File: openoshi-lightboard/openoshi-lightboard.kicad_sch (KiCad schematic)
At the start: 26 parts, among them J1 USB_C_Receptacle_PowerOnly_6P, Q1 CSD16301Q2, Q2 CSD16301Q2, Q3 CSD16301Q2, Q4 CSD16301Q2, SW1 SW_Push, SW2 SW_Push, U1 CH32V003FxUx, U2 TLV61070ADBV, U3 MCP73831-3-MC

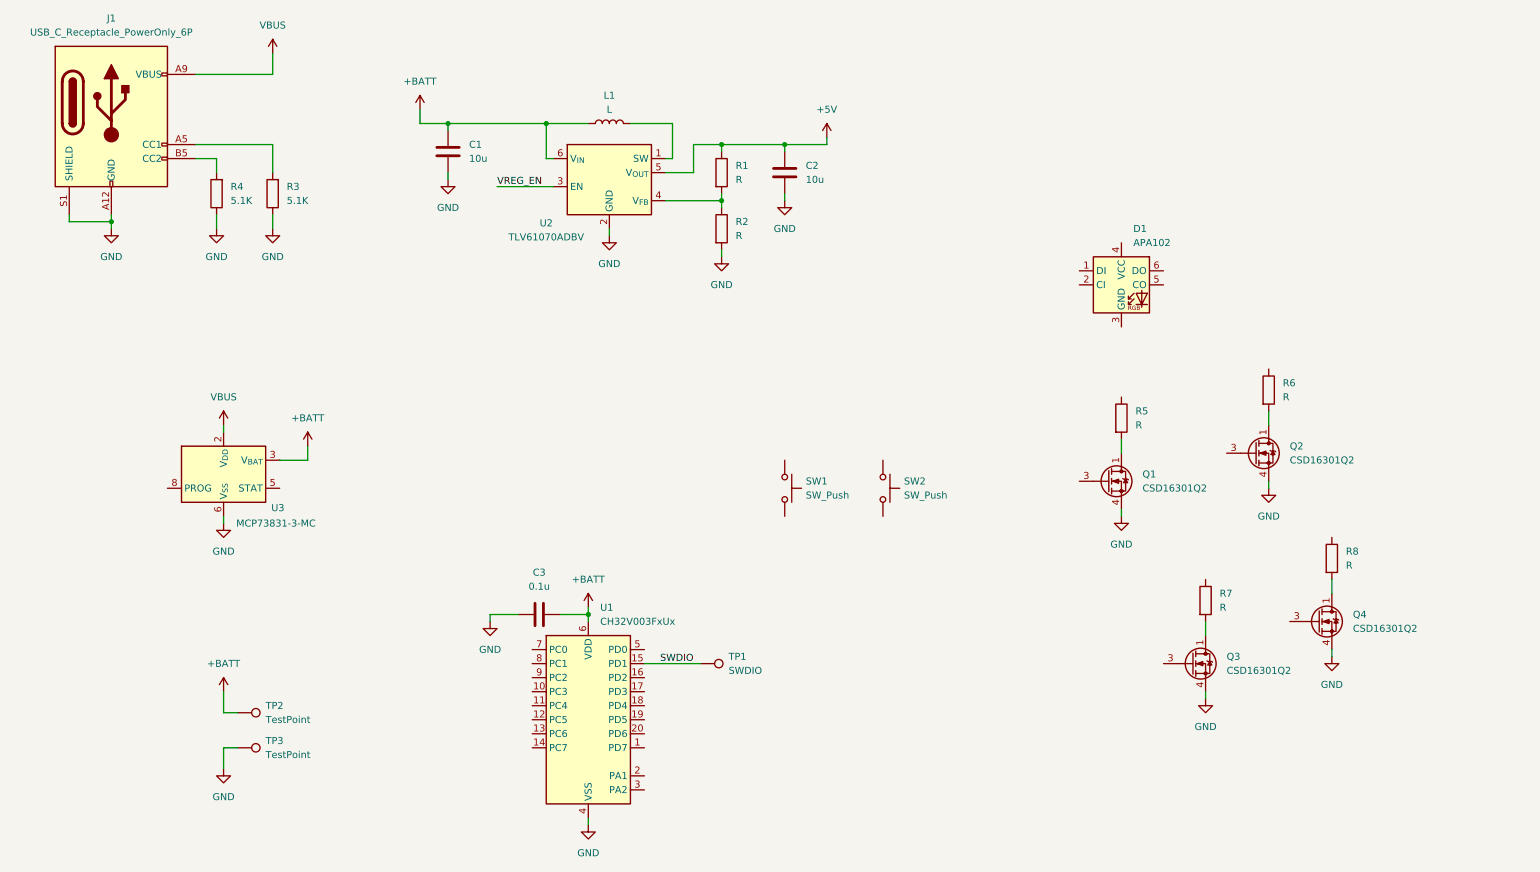
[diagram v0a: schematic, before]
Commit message: updated readme and part names
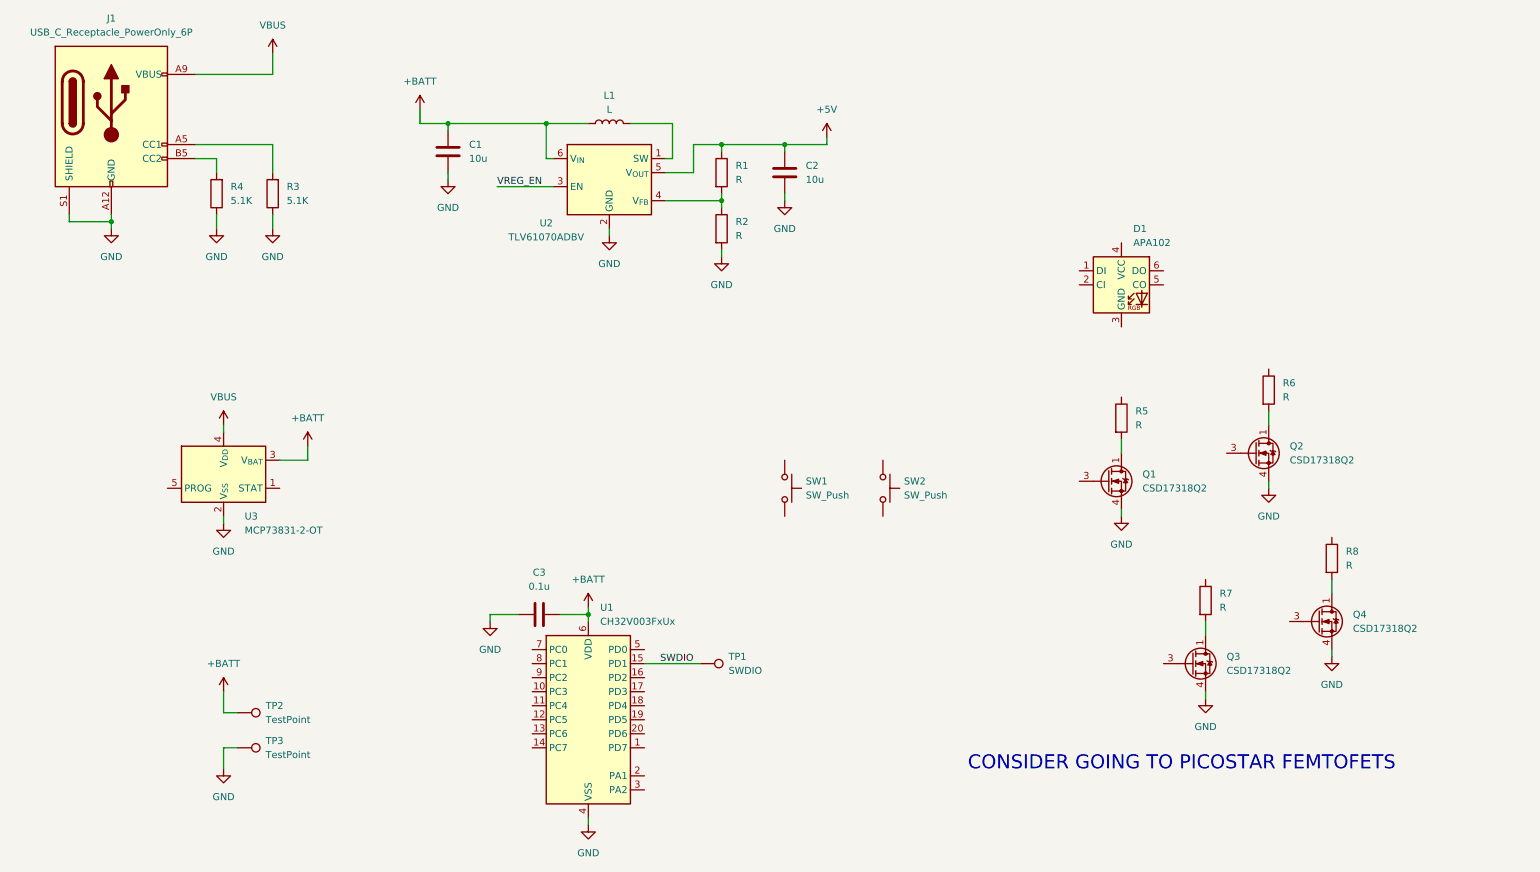
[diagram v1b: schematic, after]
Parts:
- removed U3: MCP73831-3-MC, Package_DFN_QFN:DFN-8-1EP_3x2mm_P0.5mm_EP1.7x1.4mm, symbol Battery_Management:MCP73831-3-MC
- added U3: MCP73831-2-OT, Package_TO_SOT_SMD:SOT-23-5, symbol Battery_Management:MCP73831-2-OT
- Q1, Q2, Q3, Q4: value CSD16301Q2 -> CSD17318Q2
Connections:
- net +BATT: now also U3.3 (V_{BAT})
- net GND: now also U3.2 (V_{SS})
- net VBUS: now also U3.4 (V_{DD})
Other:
- note added: "CONSIDER GOING TO PICOSTAR FEMTOFETS"

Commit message: added LED
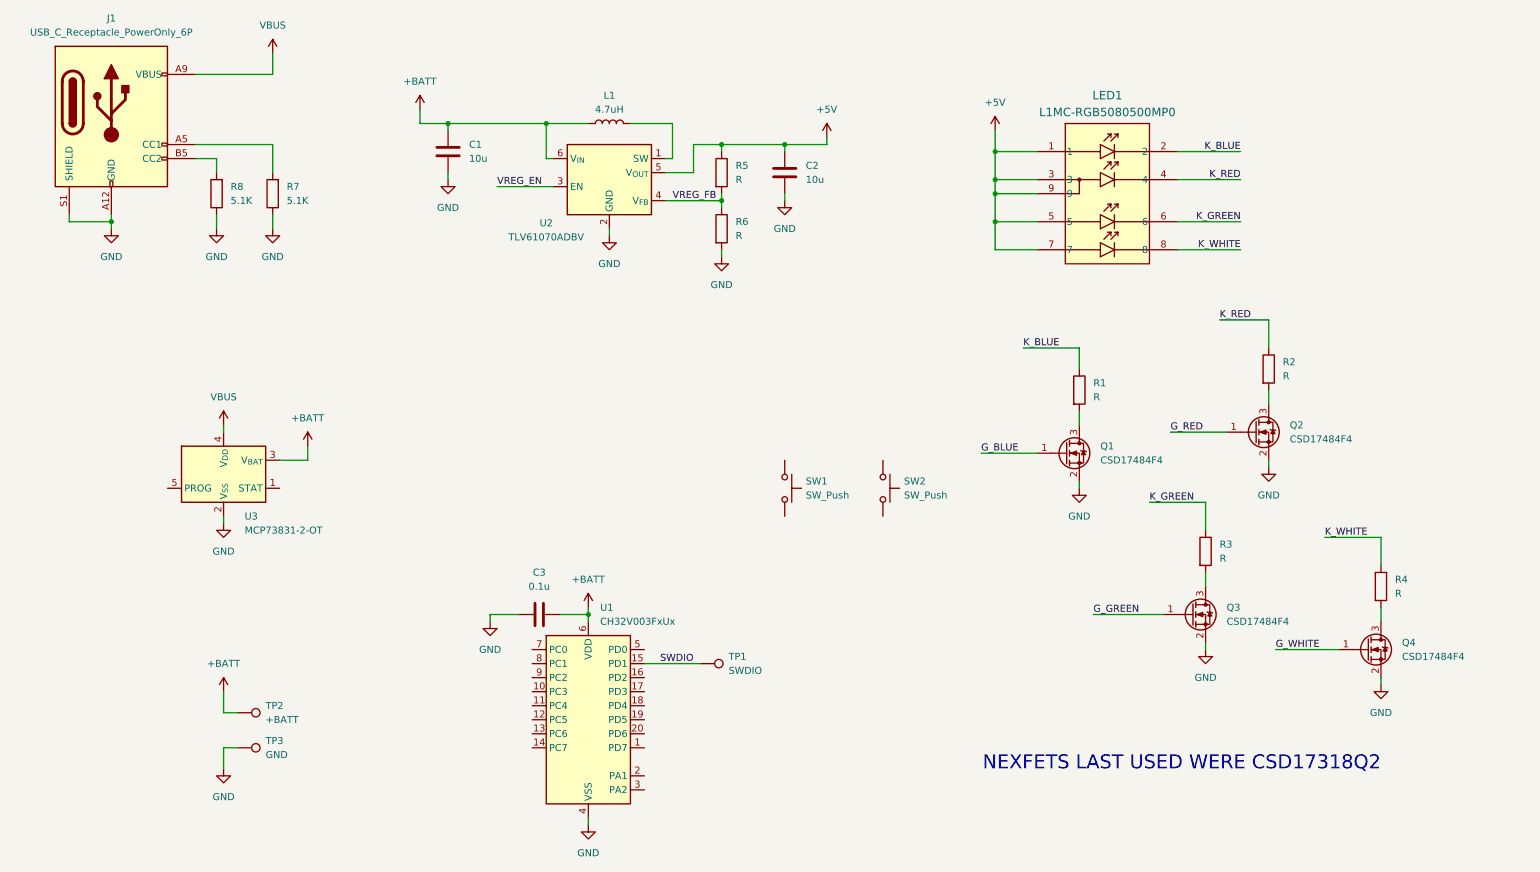
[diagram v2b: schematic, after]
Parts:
- removed D1: APA102, LED_SMD:LED_RGB_5050-6, symbol LED:APA102
- removed Q1, Q2, Q3, Q4: CSD17318Q2, Package_SON:Texas_DQK, symbol Transistor_FET:CSD16301Q2
- added LED1: L1MC-RGB5080500MP0, openoshi-lightboard:5050RGBW_LUL, symbol openoshi-lightboard:L1MC-RGB5080500MP0
- added Q1, Q2, Q3, Q4: CSD17484F4, Package_DFN_QFN:Texas_PicoStar_DFN-3_0.69x0.60mm, symbol Transistor_FET:CSD13380F3
- L1: value L -> 4.7uH
- TP2: value TestPoint -> +BATT; footprint TestPoint:TestPoint_Keystone_5019_Miniature -> Connector_Wire:SolderWirePad_1x01_SMD_5x10mm
- TP3: value TestPoint -> GND; footprint TestPoint:TestPoint_Keystone_5019_Miniature -> Connector_Wire:SolderWirePad_1x01_SMD_5x10mm
- renumbered R5 to R1, R6 to R2, R7 to R3, R8 to R4, R1 to R5, R2 to R6, R3 to R7, R4 to R8
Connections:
- net +5V: now also LED1.1, LED1.3, LED1.5, LED1.7, LED1.9
- net GND: now also Q1.2 (S), Q2.2 (S), Q3.2 (S), Q4.2 (S)
- net K_WHITE: now reaches R4.1
- net K_WHITE: now also LED1.8
- net at R4.2: now also Q4.3 (D)
- net K_RED: now reaches R2.1
- net K_RED: now also LED1.4
- net at R2.2: now also Q2.3 (D)
- net VREG_FB: now reaches R5.2, R6.1, U2.4 (V_{FB})
- net at R1.2: now also Q1.3 (D)
- net at R3.2: now also Q3.3 (D)
- net K_GREEN: now reaches R3.1
- net K_GREEN: now also LED1.6
- net K_BLUE: now reaches R1.1
- net K_BLUE: now also LED1.2
- new net G_BLUE: Q1.1 (G)
- new net G_GREEN: Q3.1 (G)
- new net G_RED: Q2.1 (G)
- new net G_WHITE: Q4.1 (G)
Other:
- note added: "NEXFETS LAST USED WERE CSD17318Q2"
- note removed: "CONSIDER GOING TO PICOSTAR FEMTOFETS"
- moved on the sheet: R1, R2, R3, R4

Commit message: Safety upgrades all around
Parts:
- removed LED1: L1MC-RGB5080500MP0, openoshi-lightboard:5050RGBW_LUL, symbol openoshi-lightboard:L1MC-RGB5080500MP0
- added D1: Lumileds_5052RGBW, openoshi-lightboard:LED_Lumileds_5052RGBW_LGA9_5.0x5.2mm_P0.5mm, symbol openoshi-lightboard:Lumileds_5052RGBW
- added R10: 2k, Resistor_SMD:R_0603_1608Metric, symbol Device:R
- added R9: 220, Resistor_SMD:R_0603_1608Metric, symbol Device:R
- J1: footprint Connector_USB:USB_C_Receptacle_GCT_USB4135-GF-A_6P_TopMnt_Horizontal -> Connector_USB:USB_C_Receptacle_GCT_USB4125-xx-x_6P_TopMnt_Horizontal
- L1: value 4.7uH -> L
- Q1, Q2, Q3, Q4: value CSD17484F4 -> PMZ600UNEYL
- R5: renamed from R1; value R -> 118; footprint Resistor_SMD:R_1206_3216Metric -> Resistor_SMD:R_0603_1608Metric
- R6: renamed from R2; value R -> 69.8; footprint Resistor_SMD:R_1206_3216Metric -> Resistor_SMD:R_0603_1608Metric
- R7: renamed from R3; value R -> 69.8; footprint Resistor_SMD:R_1206_3216Metric -> Resistor_SMD:R_0603_1608Metric
- R8: renamed from R4; value R -> 69.8; footprint Resistor_SMD:R_1206_3216Metric -> Resistor_SMD:R_0603_1608Metric
- TP2, TP3: footprint Connector_Wire:SolderWirePad_1x01_SMD_5x10mm -> TestPoint:TestPoint_Keystone_5019_Miniature
- U2: value TLV61070ADBV -> TLV61220
- renumbered R5 to R1, R6 to R2, R7 to R3, R8 to R4
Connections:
- net +5V: now also D1.1 (AB), D1.3 (AR), D1.5 (AG), D1.7 (AW), D1.9 (AR)
- net GND: now also SW1.2, SW2.2, R10.2
- net K_BLUE: now also D1.2 (KB)
- net K_GREEN: now also D1.6 (KG)
- net K_RED: now also D1.4 (KR)
- net K_WHITE: now also D1.8 (KW)
- net SWDIO: now also R9.2; no longer U1.15 (PD1)
- net SW2_DET: now reaches SW2.1
- net CHG_STAT: now reaches U3.1 (STAT)
- net at U3.5 (PROG): now also R10.1
- net SW1_DET: now reaches SW1.1
- net VREG_FB: no longer names the net of R1.2, R2.1, U2.4 (V_{FB})
- new net: R9.1, U1.15 (PD1)
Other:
- note added: "CSD17318Q2 is WSON6 alternative"
- note added: "TLV61070A is pin-compatible and allows for more output current"
- note added: "TODO CHANGE THIS TO XINGLIGHT PLCC8"
- note added: "TODO Connect VREG_EN to the MCU, configure GPIO as output push-pull"
- note added: "TODO Connect these three to the MCU, configure the GPIOs as input pullup"
- note added: "TODO connect these 4 to PWM pins"
- note removed: "NEXFETS LAST USED WERE CSD17318Q2"
- moved on the sheet: R5, R6, R7, R8, SW1, SW2, TP1

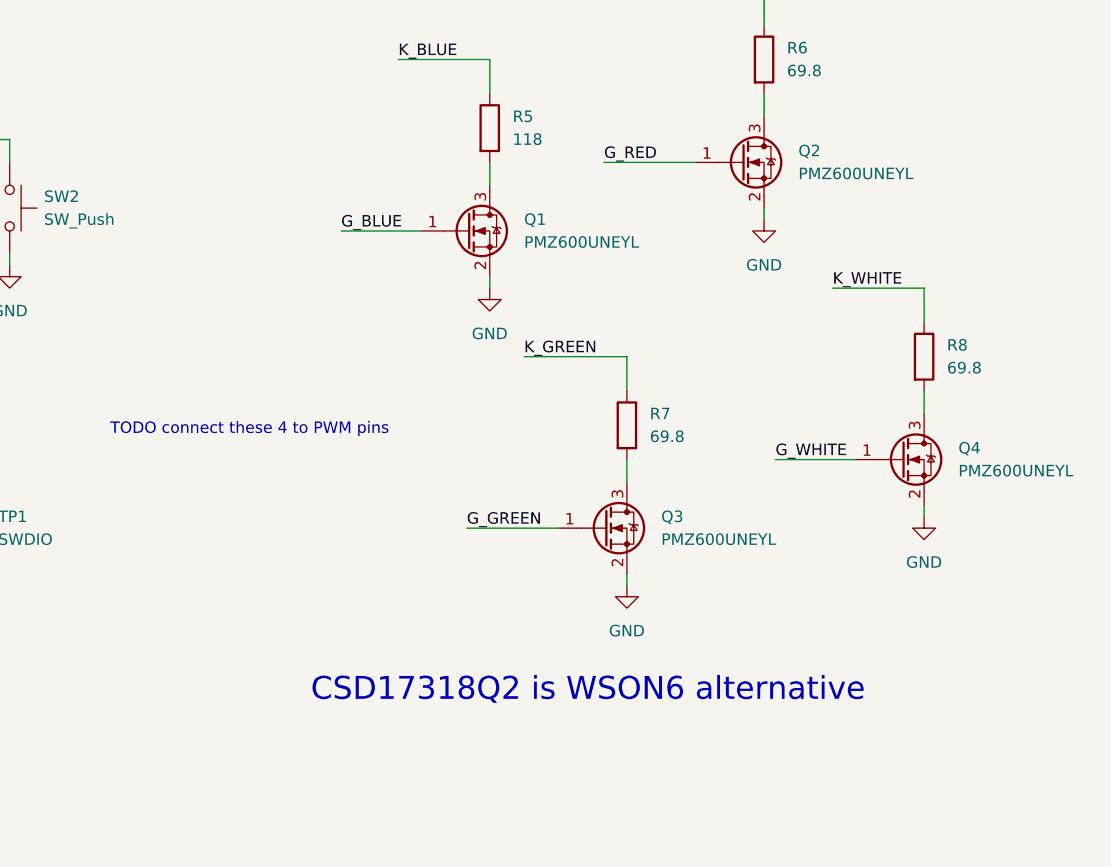
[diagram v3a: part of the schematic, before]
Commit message: Update openoshi-lightboard.kicad_sch
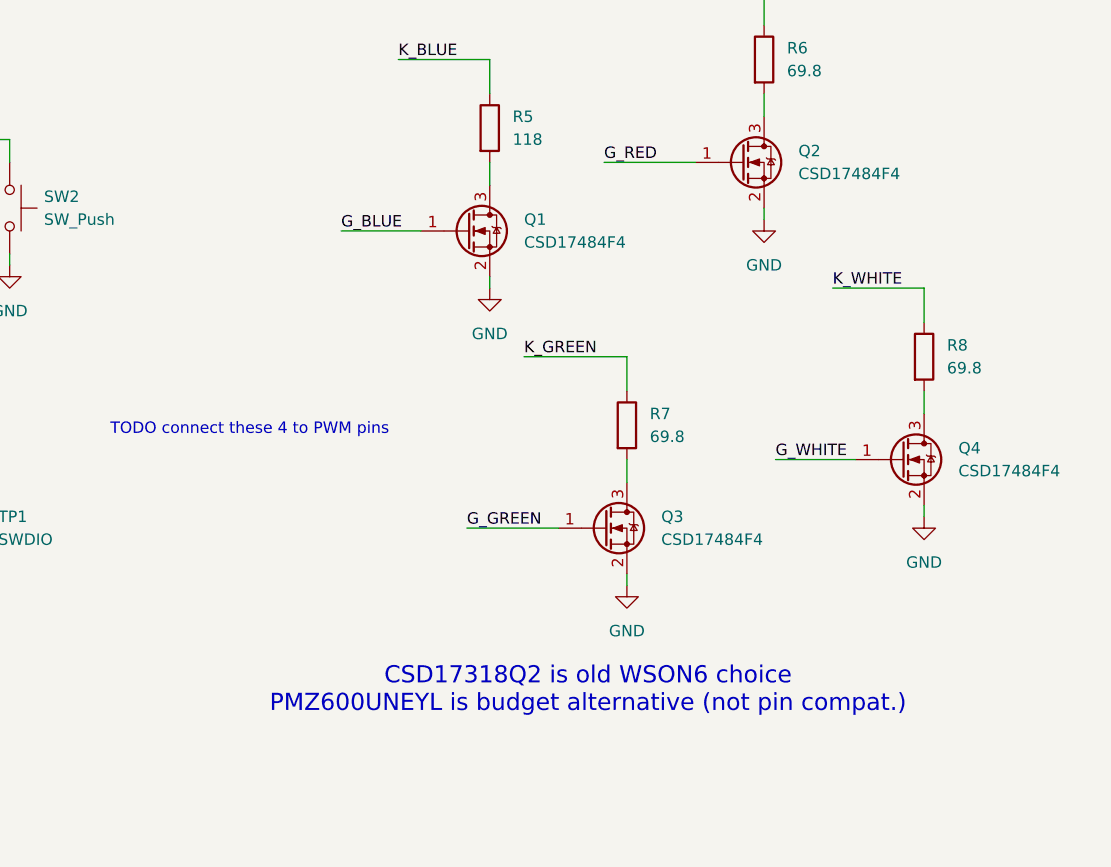
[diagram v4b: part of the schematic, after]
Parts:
- Q1, Q2, Q3, Q4: value PMZ600UNEYL -> CSD17484F4
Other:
- note added: "CSD17318Q2 is old WSON6 choice PMZ600UNEYL is budget alternative (not pin compat.)"
- note removed: "CSD17318Q2 is WSON6 alternative"
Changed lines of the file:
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@@
 		)
 	)
-	(text "CSD17318Q2 is WSON6 alternative"
+	(text "CSD17318Q2 is old WSON6 choice\nPMZ600UNEYL is budget alternative (not pin compat.)"
 		(exclude_from_sim no)
 		(at 228.092 159.004 0)
 		(effects
 			(font
-				(size 2.54 2.54)
+				(size 1.905 1.905)
 			)
 		)
@@
 			)
 		)
-		(property "Value" "PMZ600UNEYL"
+		(property "Value" "CSD17484F4"
 			(at 220.98 109.2199 0)
 			(effects
@@
 			)
 		)
-		(property "Value" "PMZ600UNEYL"
+		(property "Value" "CSD17484F4"
 			(at 236.22 142.2399 0)
 			(effects
@@
 			)
 		)
-		(property "Value" "PMZ600UNEYL"
+		(property "Value" "CSD17484F4"
 			(at 251.46 101.5999 0)
 			(effects
@@
 			)
 		)
-		(property "Value" "PMZ600UNEYL"
+		(property "Value" "CSD17484F4"
 			(at 269.24 134.6199 0)
 			(effects
